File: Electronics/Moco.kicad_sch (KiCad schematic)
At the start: 38 parts, among them J1 Conn_01x04, J2 Conn_01x01, J3 Conn_ARM_JTAG_SWD_10, J4 Conn_01x03, J5 Conn_01x01, J6 Conn_01x04, J8 Conn_01x01, J9 Conn_01x01, U1 EFM32PG22C200FxxIM32, U2 SP485EN, U3 TMAG5273, U4 DRV8311, Y1 ECS-384-CDX-1983

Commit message: New design with ESP32-C3
This design swaps the EFM32PG22 for an ESP32-C3. This reduces cost
and improves availability. It also lets me use USB and CANbus instead
of RS485.
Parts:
- removed C16: 0.1 + 2.7 uF 6.3V X5R, Capacitor_SMD:C_0402_1005Metric, symbol Device:C_Small
- removed C2, C3: 0.1 uF 6.3V X5R, Capacitor_SMD:C_0402_1005Metric, symbol Device:C_Small
- removed C4: 0.1 + 1 uF 6.3V X5R, Capacitor_SMD:C_0402_1005Metric, symbol Device:C_Small
- removed C6: 0.01 + 1 uF 6.3V X5R, Capacitor_SMD:C_0402_1005Metric, symbol Device:C_Small
- removed J1: Conn_01x04, Connector_PinHeader_2.54mm:PinHeader_1x04_P2.54mm_Vertical, symbol Connector_Generic:Conn_01x04
- removed J2, J5: Conn_01x01, Library:Pad_CircularEdge_Ro16.5Ri15_Single, symbol Connector_Generic:Conn_01x01
- removed J3: Conn_ARM_JTAG_SWD_10, Connector_PinHeader_1.00mm:PinHeader_2x05_P1.00mm_Vertical, symbol Connector:Conn_ARM_JTAG_SWD_10
- removed TP1, TP2, TP3, TP4, TP5: TestPoint, TestPoint:TestPoint_Pad_1.0x1.0mm, symbol Connector:TestPoint
- removed U1: EFM32PG22C200FxxIM32, Package_DFN_QFN:QFN-32-1EP_4x4mm_P0.4mm_EP2.9x2.9mm, symbol Library:EFR32BG22C200FxxIM32
- removed U2: SP485EN, Package_SO:SOIC-8_3.9x4.9mm_P1.27mm, symbol DStutman_Interface:SP485EN
- added C14, C17, C18, C19, C20, C21, C22, C23, C24, C25: C_Small, Capacitor_SMD:C_0402_1005Metric, symbol Device:C_Small
- added C26, C27: 10uF, Capacitor_SMD:C_0805_2012Metric, symbol Device:C_Small
- added C28: 0.1uF, Capacitor_SMD:C_0402_1005Metric, symbol Device:C_Small
- added C29, C30, C31: 22uF, Capacitor_SMD:C_0805_2012Metric, symbol Device:C_Small
- added J3: USB_C_Receptacle_USB2.0, Connector_USB:USB_C_Receptacle_JAE_DX07S016JA1R1500, symbol Connector:USB_C_Receptacle_USB2.0
- added L2: 3.3uH 114mR, Inductor_SMD:L_0805_2012Metric, symbol Device:L_Small
- added R10, R11: 22R, Resistor_SMD:R_0402_1005Metric, symbol Device:R_Small_US
- added R5: R_Small_US, Resistor_SMD:R_0402_1005Metric, symbol Device:R_Small_US
- added R6: 33.2kR, Resistor_SMD:R_0402_1005Metric, symbol Device:R_Small_US
- added R7: 10kR, Resistor_SMD:R_0402_1005Metric, symbol Device:R_Small_US
- added R8, R9: 5.1kR, Resistor_SMD:R_0402_1005Metric, symbol Device:R_Small_US
- added U1: ESP32-C3, Package_DFN_QFN:QFN-32-1EP_5x5mm_P0.5mm_EP3.45x3.45mm, symbol Library:ESP32-C3
- added U2: TPS562201, Package_TO_SOT_SMD:SOT-23-6, symbol Library:TPS562201
- added U5: TJA1462ATK/0Z, Package_SON:HVSON-8-1EP_3x3mm_P0.65mm_EP1.6x2.4mm, symbol Library:TJA1462ATK/0Z
- C1: value (none) -> C_Small
- C12: value 1uF 6.3V X7R -> 0.1uF 6.3V X7R
- C13, C15: footprint Capacitor_SMD:C_1206_3216Metric -> Capacitor_SMD:C_0805_2012Metric
- J4: footprint Connector_PinHeader_2.54mm:PinHeader_1x03_P2.54mm_Horizontal -> Connector_PinHeader_2.54mm:PinHeader_1x03_P2.54mm_Vertical
- J6: footprint Connector_PinHeader_2.54mm:PinHeader_1x04_P2.54mm_Vertical -> Connector_JST:JST_SH_BM04B-SRSS-TB_1x04-1MP_P1.00mm_Vertical
- R1, R2: value 910kR -> 910R
- Y1: value ECS-384-CDX-1983 -> XTAL
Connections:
- net +3V3: now also C1.1, C12.1, C18.1, C21.1, C22.1, C23.1, C24.1, C29.2, C30.2, C31.2, L2.2, R6.1, U1.11 (VDD3P3_RTC), U1.17 (VDD3P3_CPU), U1.2 (VDD3P3), U1.3 (VDD3P3), U1.31 (VDDA), U1.32 (VDDA), U5.5 (VIO); no longer C10.1, U4.17 (AVDD)
- net +5V: now also U5.3 (VCC); no longer C12.1
- net DRV_~{SCS}: now also U1.23 (SPID/GPIO16)
- net GND: now also C1.2, C14.2, C17.1, C18.2, C19.2, C20.2, C21.2, C22.2, C23.2, C24.2, C25.1, C26.2, C27.2, C29.1, C30.1, C31.1, J3.A1 (GND), J3.A12 (GND), J3.B1 (GND), J3.B12 (GND), J3.S1 (SHIELD), R7.2, R8.1, R9.1, U1.33 (GND), U2.1 (GND), U5.2 (GND), U5.9 (GND); no longer C1.1
- net PWM_SYNC: now also U1.24 (SPIQ/GPIO17)
- net SCLK: now also U1.20 (SPIWP/GPIO13)
- net SDI: now also U1.21 (SPICS0/GPIO14)
- net SDO: now also U1.22 (SPICLK/GPIO15)
- net SOA: now also C14.1, U1.4 (XTAL_32K_P/ADC1_CH0)
- net SOB: now also C17.2, U1.5 (XTAL_32K_N/ADC1_CH1)
- net SOC: now also C25.2, U1.6 (GPIO2/ADC1_CH2)
- net TMS_SCL: now also U1.19 (SPIHD/GPIO12)
- net TMS_SDA: now also U1.18 (VDD_SPI/GPIO11)
- net Vdrive: now also C26.1, C27.1, U2.3 (VIN), U2.5 (EN)
- net ~{RESET}: now also U1.7 (CHIP_EN)
- net at Y1.1: now also C20.1, R5.1
- net at Y1.3: now also C19.1, U1.29 (XTAL_N)
- net at D1.2 (A): now also U1.8 (GPIO3/ADC1_CH3)
- net RS485_A renamed CANH
- net CANH: now also U5.7 (CANH)
- net RS485_B renamed CANL
- net CANL: now also U5.6 (CANL)
- net ~{INT}: no longer names the net of U3.5 (~{INT})
- new net: C28.1, L2.1, U2.2 (SW)
- new net: R6.2, R7.1, U2.4 (VFB)
- new net: C28.2, U2.6 (VBST)
- new net: R5.2, U1.30 (XTAL_P)
- new net: J3.B5 (CC2), R9.2
- new net: J3.A5 (CC1), R8.2
- new net: J3.A4 (VBUS), J3.A9 (VBUS), J3.B4 (VBUS), J3.B9 (VBUS)
- new net: C10.1, U4.17 (AVDD)
- new net CAN_EN: U1.16 (GPIO10), U5.8 (STB)
- new net CAN_RX: U1.14 (GPIO8), U5.4 (RXD)
- new net CAN_TX: U1.15 (GPIO9/BOOT), U5.1 (TXD)
- new net USB_CONN_DN: J3.A7 (D-), J3.B7 (D-), R10.2
- new net USB_CONN_DP: J3.A6 (D+), J3.B6 (D+), R11.2
- new net USB_DN: R10.1, U1.25 (GPIO18/USB_D-)
- new net USB_DP: R11.1, U1.26 (GPIO19/USB_D+)
- no-connect marks 4 -> 12
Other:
- note added: "CANbus"
- note added: "Regulator"
- note added: "~{INT} not used. Isochronous reads from sensor."
- note removed: "10-GND"
- note removed: "13-GND"
- note removed: "28-GND"
- note removed: "29-GND"
- note removed: "30-GND"
- note removed: "Bus out"
- note removed: "Debug/Prog Connector"
- note removed: "Expansion Connectors"
- note removed: "Locating Holes"
- note removed: "Only ESD protection is chip-internal"
- note removed: "REMOVED Edge notch substituted"
- note removed: "RS485"
- note removed: "USER NOTE Intended for use with M2 pins in motor mount. Prevent rotational movement of board (and thus encoder)."
- note removed: "USER NOTE RS485 GND provided in-case two bus members are operating from different supplies. All connected boards must have same GND potential or be floating. Otherwise bad things will happen."
- note removed: "Uses internal pullup, keep trace capacitance low"
- moved on the sheet: C10, C11, C12, C13, C15, C5, C7, C8, C9, D1, J4, J6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

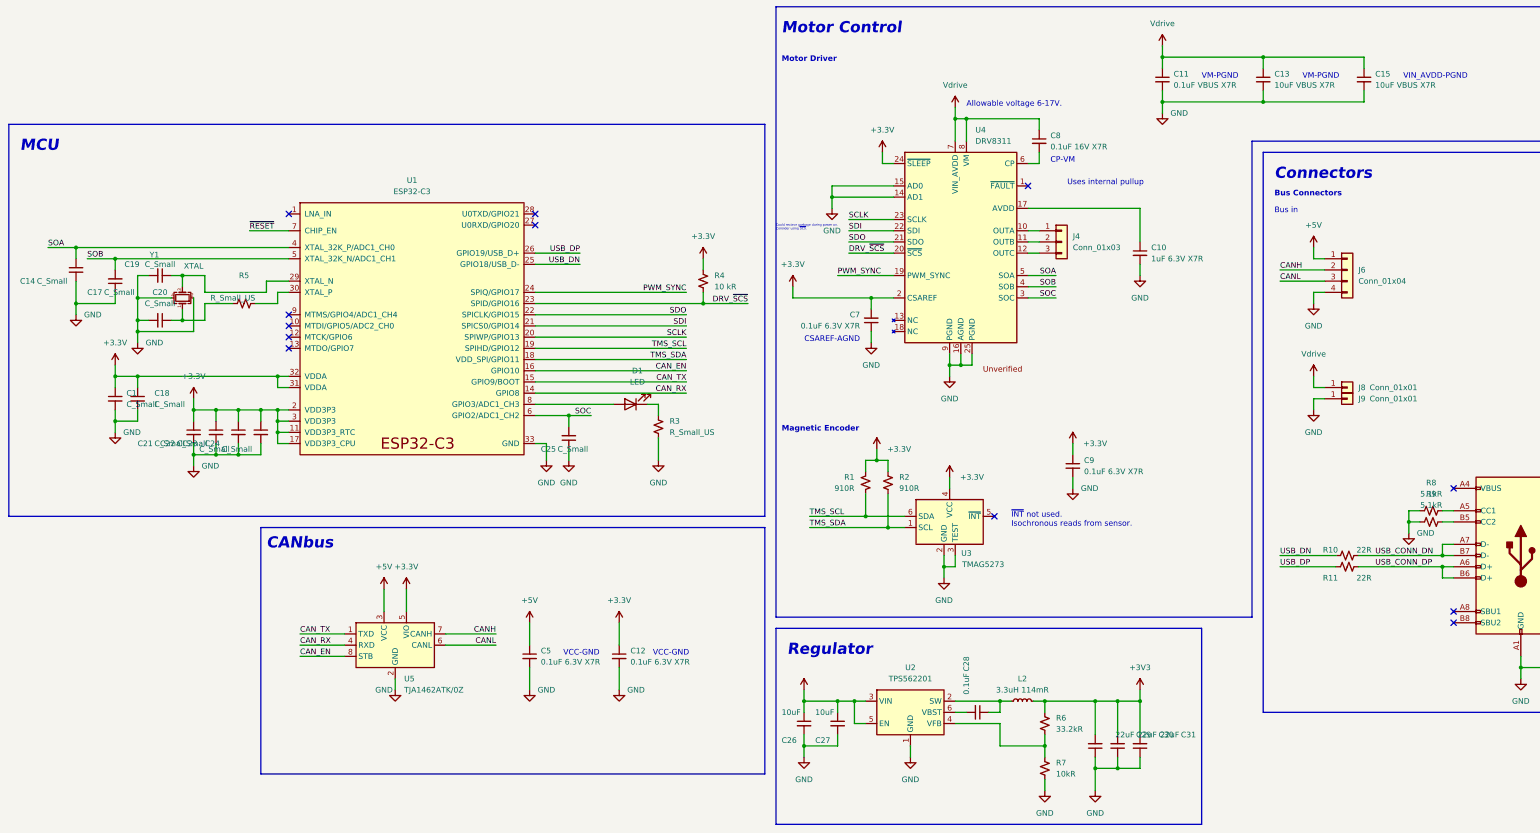
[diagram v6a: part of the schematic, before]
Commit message: Complete ESP32-C3 redesign
- Remove status LED to free up pin
- Avoid using embedded flash SPI pins
- Update silkscreen
- Improve I2C and CANbus pin assignments
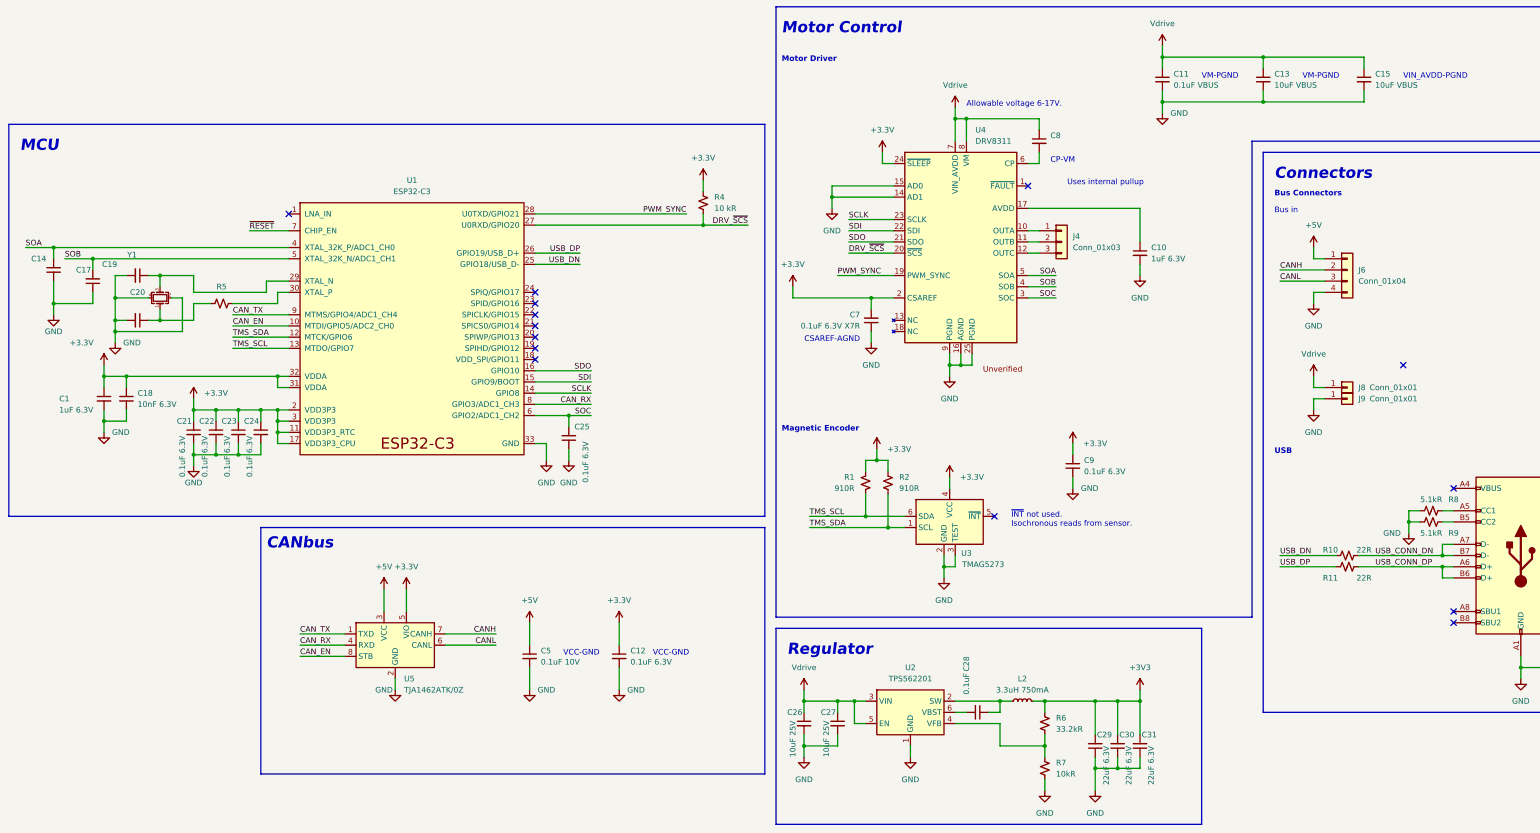
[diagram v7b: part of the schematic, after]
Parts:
- removed D1: LED, LED_SMD:LED_0402_1005Metric, symbol Device:LED
- removed R3: R_Small_US, Resistor_SMD:R_0402_1005Metric, symbol Device:R_Small_US
- C1: value C_Small -> 1uF 6.3V
- C10: value 1uF 6.3V X7R -> 1uF 6.3V
- C11: value 0.1uF VBUS X7R -> 0.1uF VBUS
- C12, C9: value 0.1uF 6.3V X7R -> 0.1uF 6.3V
- C13, C15: value 10uF VBUS X7R -> 10uF VBUS
- C14, C17, C19, C20: value C_Small -> (none)
- C18: value C_Small -> 10nF 6.3V
- C21, C22, C23, C24, C25: value C_Small -> 0.1uF 6.3V
- C26, C27: value 10uF -> 10uF 25V
- C29, C30, C31: value 22uF -> 22uF 6.3V
- C5: value 0.1uF 6.3V X7R -> 0.1uF 10V
- C8: value 0.1uF 16V X7R -> (none)
- L2: value 3.3uH 114mR -> 3.3uH 750mA
- R5: value R_Small_US -> (none)
- Y1: value XTAL -> (none)
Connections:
- net CAN_EN: now also U1.10 (MTDI/GPIO5/ADC2_CH0); no longer U1.16 (GPIO10)
- net CAN_RX: now also U1.8 (GPIO3/ADC1_CH3); no longer U1.14 (GPIO8)
- net CAN_TX: now also U1.9 (MTMS/GPIO4/ADC1_CH4); no longer U1.15 (GPIO9/BOOT)
- net DRV_~{SCS}: now also U1.27 (U0RXD/GPIO20); no longer U1.23 (SPID/GPIO16)
- net PWM_SYNC: now also U1.28 (U0TXD/GPIO21); no longer U1.24 (SPIQ/GPIO17)
- net SCLK: now also U1.14 (GPIO8); no longer U1.20 (SPIWP/GPIO13)
- net SDI: now also U1.15 (GPIO9/BOOT); no longer U1.21 (SPICS0/GPIO14)
- net SDO: now also U1.16 (GPIO10); no longer U1.22 (SPICLK/GPIO15)
- net TMS_SCL: now also U1.13 (MTDO/GPIO7); no longer U1.19 (SPIHD/GPIO12)
- net TMS_SDA: now also U1.12 (MTCK/GPIO6); no longer U1.18 (VDD_SPI/GPIO11)
- no-connect marks 12 -> 14
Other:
- note added: "USB"
- note removed: "Could recieve garbage during power on. Consider using ~{SCS}."
- moved on the sheet: C1, C14, C17, C18, C19, C20, R5, Y1

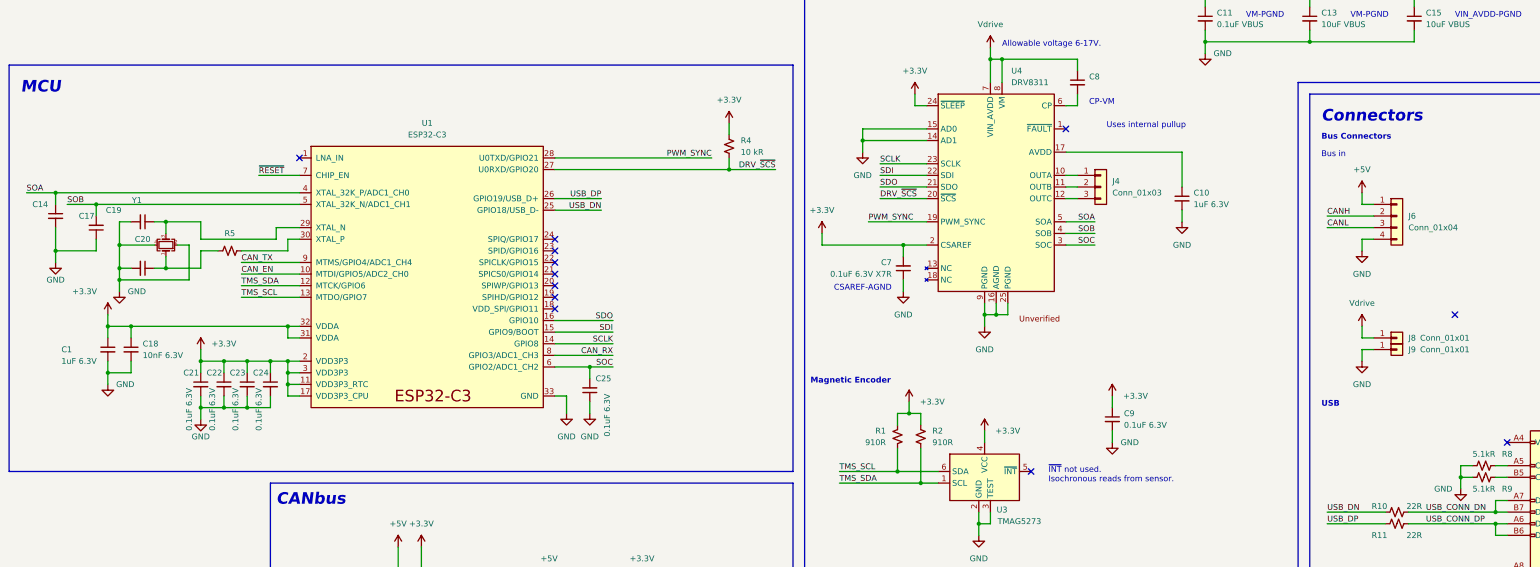
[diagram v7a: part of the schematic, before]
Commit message: Correct I2C net labels, add NRESET pad
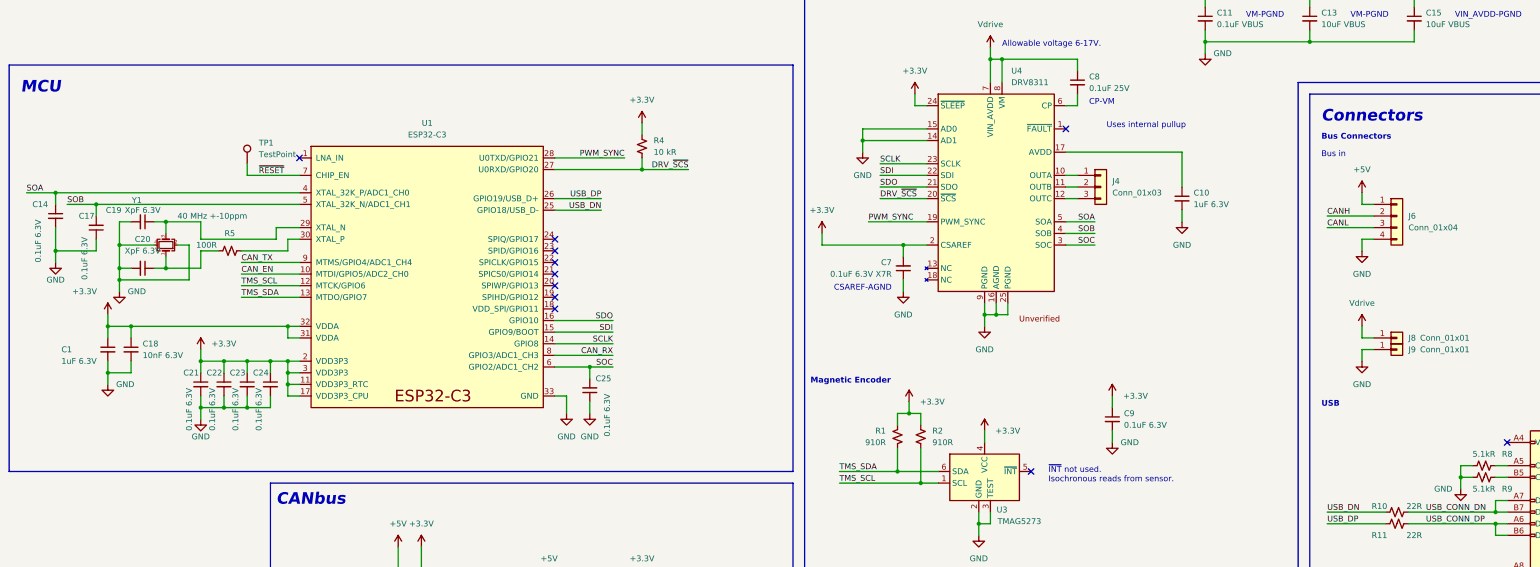
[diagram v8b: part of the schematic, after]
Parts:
- added TP1: TestPoint, TestPoint:TestPoint_Pad_1.5x1.5mm, symbol Connector:TestPoint
- C14, C17: value (none) -> 0.1uF 6.3V
- C19, C20: value (none) -> XpF 6.3V
- C8: value (none) -> 0.1uF 25V
- R5: value (none) -> 100R
- Y1: value (none) -> 40 MHz +-10ppm
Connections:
- net TMS_SCL: now also R2.2, U1.12 (MTCK/GPIO6), U3.1 (SCL); no longer R1.1, U1.13 (MTDO/GPIO7), U3.6 (SDA)
- net TMS_SDA: now also R1.1, U1.13 (MTDO/GPIO7), U3.6 (SDA); no longer R2.2, U1.12 (MTCK/GPIO6), U3.1 (SCL)
- net ~{RESET}: now also TP1.1
- no-connect marks 14 -> 13
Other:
- moved on the sheet: R4
